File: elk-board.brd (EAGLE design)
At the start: 55 x 25.6 mm, 199 parts, among them IC1 KLM8G1GESD-B03P, IC10 MP2143DJ-LF-P, IC2 ALLWINNER--H3, IC3 SY6280, IC4 K4B4G1646D-BCK0, IC5 RT8059GJ5, IC6 RT8059GJ5, IC7 SY8089A, IC8 NCP803SN263T1G, IC9 RT8059GJ5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

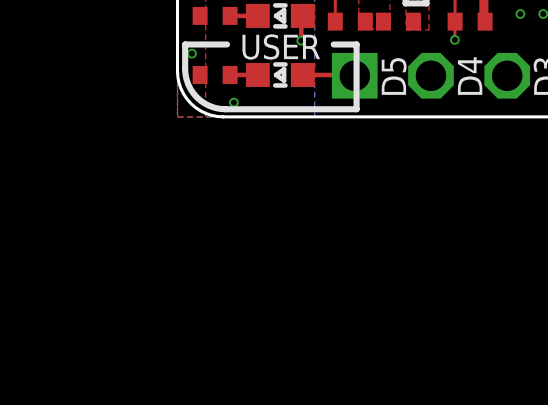
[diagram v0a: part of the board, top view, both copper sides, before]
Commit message: Added External Oscillator to MCU Schematics
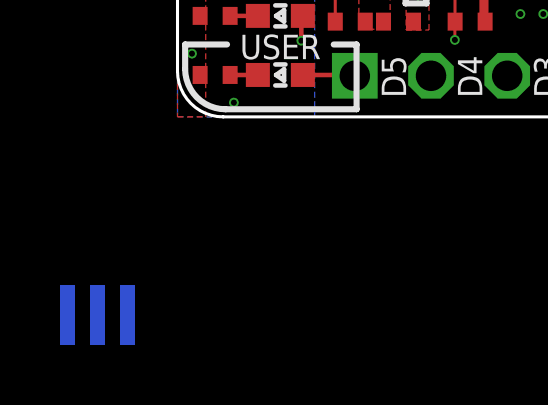
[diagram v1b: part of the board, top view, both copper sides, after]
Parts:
- added Y3: CSTCW25M0X53-R0, Tolba_Resonators:CSTCW25M0X53-R0
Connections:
- new net N$15: U2.5, Y3.IN
- new net N$16: U2.6, Y3.OUT
- net GND: now also Y3.GND
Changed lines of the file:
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@@
 <drawing>
 <settings>
-<setting alwaysvectorfont="yes"/>
+<setting alwaysvectorfont="no"/>
 <setting verticaltext="up"/>
 </settings>
 <grid distance="5" unitdist="mil" unit="mil" style="lines" multiple="1" display="no" altdistance="1" altunitdist="mil" altunit="mil"/>
 <layers>
-<layer number="1" name="Top" color="4" fill="1" visible="yes" active="yes"/>
+<layer number="1" name="Top" color="4" fill="1" visible="no" active="yes"/>
 <layer number="2" name="GND1" color="62" fill="1" visible="no" active="yes"/>
-<layer number="3" name="SIG1_RAM" color="42" fill="1" visible="yes" active="yes"/>
+<layer number="3" name="SIG1_RAM" color="42" fill="1" visible="no" active="yes"/>
 <layer number="4" name="GND2" color="63" fill="1" visible="no" active="yes"/>
 <layer number="5" name="Route5" color="19" fill="1" visible="no" active="no"/>
@@
 <layer number="11" name="Route11" color="30" fill="1" visible="no" active="no"/>
 <layer number="12" name="Route12" color="20" fill="1" visible="no" active="no"/>
-<layer number="13" name="PWR" color="16" fill="1" visible="yes" active="yes"/>
-<layer number="14" name="SIG2_RAM" color="22" fill="1" visible="yes" active="yes"/>
+<layer number="13" name="PWR" color="16" fill="1" visible="no" active="yes"/>
+<layer number="14" name="SIG2_RAM" color="22" fill="1" visible="no" active="yes"/>
 <layer number="15" name="GND3" color="21" fill="1" visible="no" active="yes"/>
 <layer number="16" name="Bottom" color="1" fill="1" visible="yes" active="yes"/>
-<layer number="17" name="Pads" color="2" fill="1" visible="yes" active="yes"/>
+<layer number="17" name="Pads" color="2" fill="1" visible="no" active="yes"/>
 <layer number="18" name="Vias" color="2" fill="1" visible="yes" active="yes"/>
 <layer number="19" name="Unrouted" color="6" fill="1" visible="yes" active="yes"/>
 <layer number="20" name="Dimension" color="24" fill="1" visible="yes" active="yes"/>
-<layer number="21" name="tPlace" color="7" fill="1" visible="yes" active="yes"/>
-<layer number="22" name="bPlace" color="7" fill="1" visible="no" active="yes"/>
-<layer number="23" name="tOrigins" color="15" fill="1" visible="yes" active="yes"/>
+<layer number="21" name="tPlace" color="7" fill="1" visible="no" active="yes"/>
+<layer number="22" name="bPlace" color="7" fill="1" visible="yes" active="yes"/>
+<layer number="23" name="tOrigins" color="15" fill="1" visible="no" active="yes"/>
 <layer number="24" name="bOrigins" color="15" fill="1" visible="yes" active="yes"/>
 <layer number="25" name="tNames" color="7" fill="1" visible="yes" active="yes"/>
@@
 <layer number="49" name="Reference" color="7" fill="1" visible="no" active="yes"/>
 <layer number="50" name="dxf" color="7" fill="1" visible="no" active="no"/>
-<layer number="51" name="tDocu" color="7" fill="1" visible="yes" active="yes"/>
-<layer number="52" name="bDocu" color="7" fill="1" visible="no" active="yes"/>
+<layer number="51" name="tDocu" color="7" fill="1" visible="no" active="yes"/>
+<layer number="52" name="bDocu" color="7" fill="1" visible="yes" active="yes"/>
 <layer number="53" name="tGND_GNDA" color="7" fill="9" visible="no" active="no"/>
 <layer number="54" name="bGND_GNDA" color="1" fill="9" visible="no" active="no"/>
@@
 <attribute name="VALUE" x="52.73675" y="5.0847" size="0.8128" layer="27" font="vector" ratio="12" align="bottom-center"/>
 </element>
+<element name="Y3" library="Tolba_Resonators" package="CSTCW25M0X53-R0" value="CSTCW25M0X53-R0" x="-2.667" y="-6.604" smashed="yes" rot="MR0">
+<attribute name="NAME" x="-2.667" y="-4.953" size="0.8128" layer="26" font="vector" ratio="15" rot="MR0" align="center"/>
+</element>
 </elements>
 <signals>
@@
 <contactref element="R21" pad="2"/>
 <via x="33.909" y="21.7424" extent="1-16" drill="0.2"/>
+<contactref element="Y3" pad="GND"/>
 <wire x1="11.811" y1="16.5989" x2="11.422" y2="17.78" width="0" layer="19" extent="1-1"/>
+<wire x1="-2.667" y1="-6.604" x2="1.8796" y2="0.47625" width="0" layer="19" extent="16-16"/>
 </signal>
 <signal name="N$1" class="9">
@@
 <via x="52.705" y="5.207" extent="1-16" drill="0.2"/>
 </signal>
+<signal name="N$15">
+<contactref element="Y3" pad="IN"/>
+<contactref element="U2" pad="5"/>
+<wire x1="-3.667" y1="-6.604" x2="45.8502" y2="8.3734" width="0" layer="19" extent="16-16"/>
+</signal>
+<signal name="N$16">
+<contactref element="U2" pad="6"/>
+<contactref element="Y3" pad="OUT"/>
+<wire x1="-1.667" y1="-6.604" x2="45.8502" y2="8.8734" width="0" layer="19" extent="16-16"/>
+</signal>
 </signals>

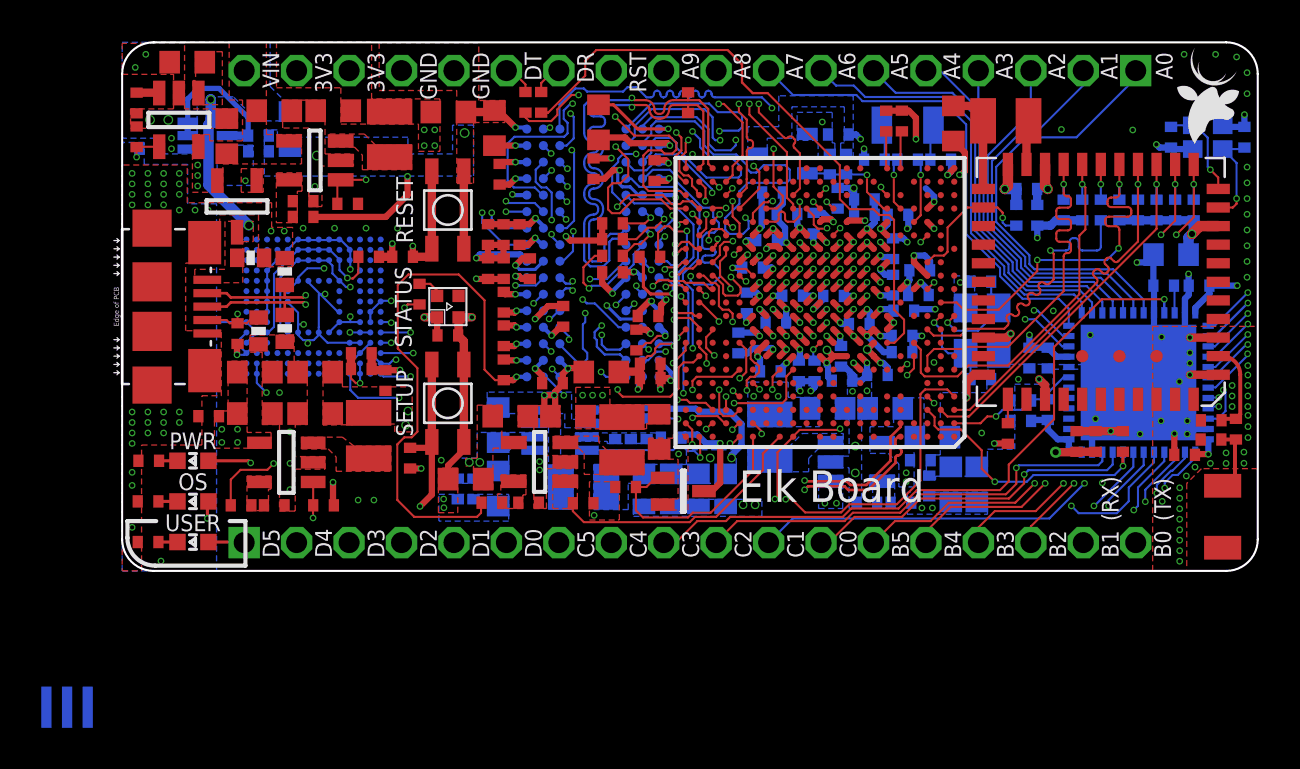
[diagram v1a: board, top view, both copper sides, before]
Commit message: Modified USB Diff Pair Impedence and Length Matching
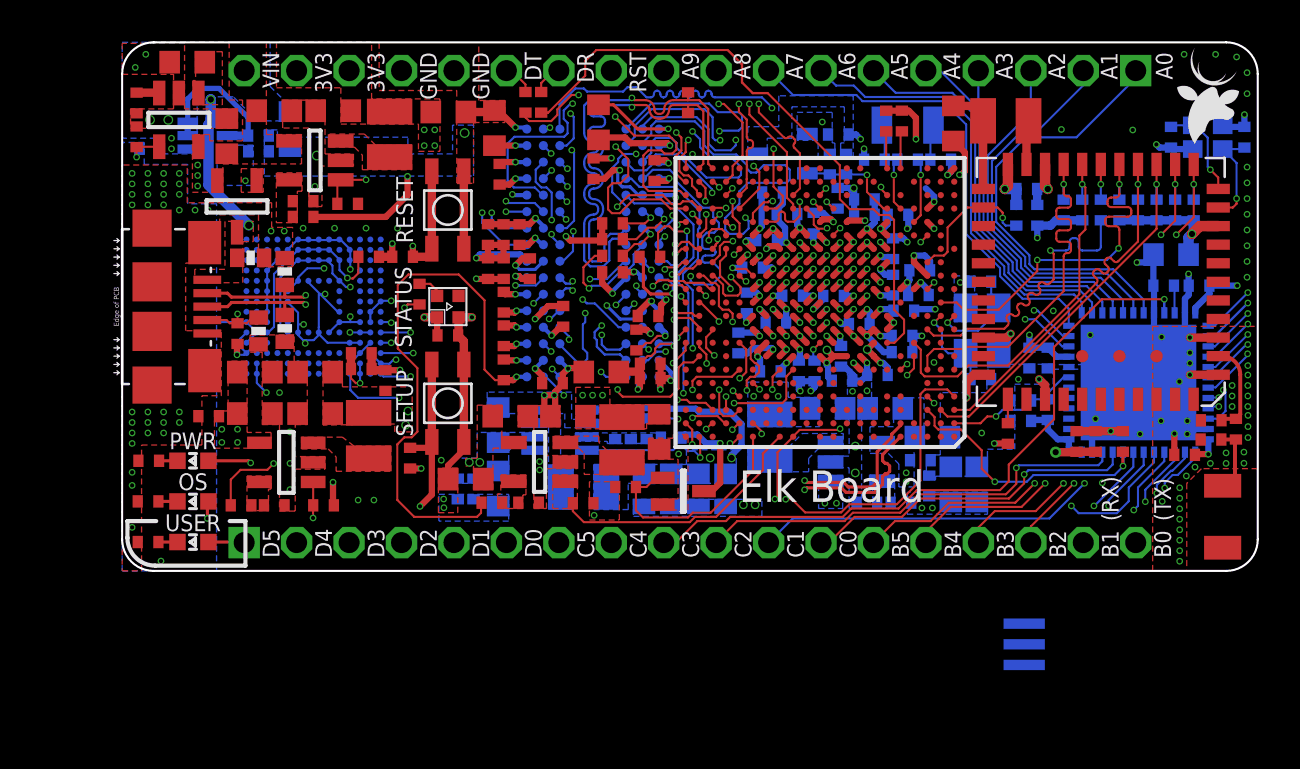
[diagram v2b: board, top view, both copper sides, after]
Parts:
- moved Y3 46.5 mm to (43.7, -3.56), turned to 270 degrees
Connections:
- net USB0_P renamed USB0

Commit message: 90ohm Impedence Control Enhancment
USB Differenctial Pair
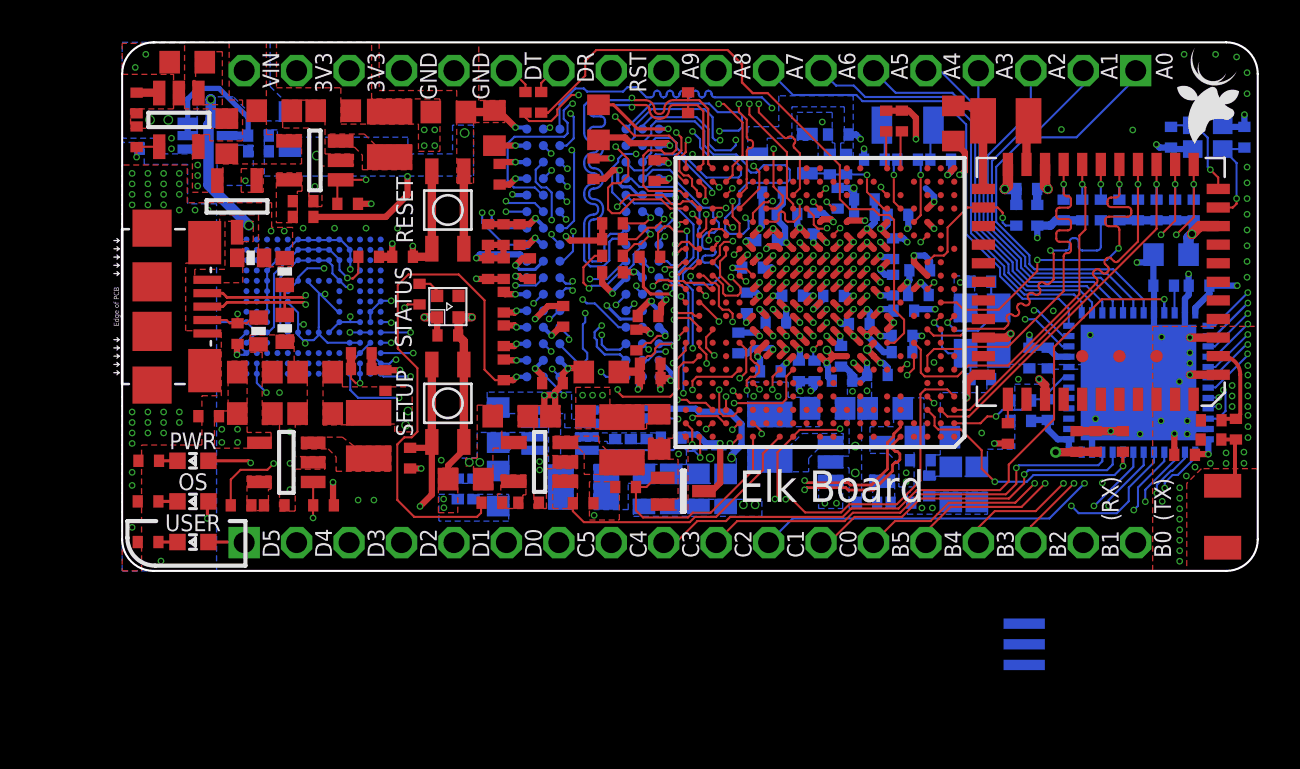
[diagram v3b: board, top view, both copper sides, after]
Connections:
- net USB0 renamed USB0_P
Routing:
- net GND: track 197.1 -> 197.8 mm, vias 224 -> 225
